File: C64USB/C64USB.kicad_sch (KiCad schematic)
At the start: 31 parts, among them J1 Keyboard, J2 USB_B_Micro, J3 AVR-ISP-6, J4 Joystick1, J5 Joystick2, J6 LED, U2 ATmega88-20A, Y1 16MHz

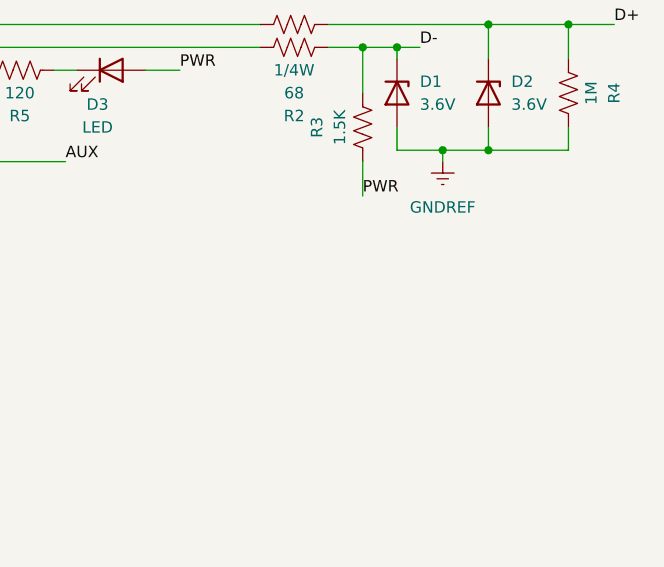
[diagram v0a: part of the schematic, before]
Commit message: Clamp D- pull up voltage
Clamps the D- pull up to ~3.3V using the simple technique of two
1N4148 diodes. Some USB host controllers are sensitive to the D- line
being pulled up to 5V (even with the 1.5K pull up resistor) and will
refuse to enumerate the device if it does so. For some reason, the TVS
diodes are not clamping the output to 3.6V.

This was particularly noticed when using the board with a Raspberry Pi
4.
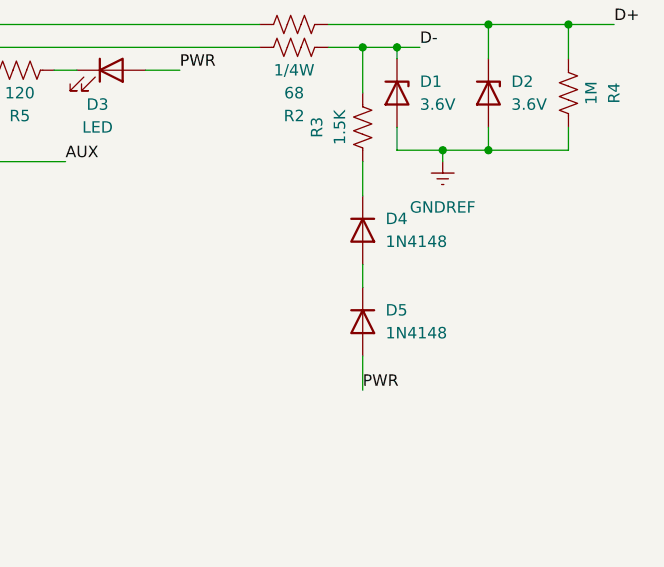
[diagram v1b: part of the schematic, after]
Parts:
- added D4, D5: 1N4148, Diode_SMD:D_SOD-123, symbol Device:D
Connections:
- net PWR: now also D5.2 (A); no longer R3.2
- new net: D4.1 (K), R3.2
- new net: D4.2 (A), D5.1 (K)
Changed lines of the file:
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@@
 	(wire
 		(pts
+			(xy 247.65 140.97) (xy 247.65 143.51)
+		)
+		(stroke
+			(width 0)
+			(type default)
+		)
+	)
+	(wire
+		(pts
 			(xy 213.36 46.99) (xy 213.36 49.53)
 		)
@@
 	(wire
 		(pts
+			(xy 247.65 151.13) (xy 247.65 154.94)
+		)
+		(stroke
+			(width 0)
+			(type default)
+		)
+	)
+	(wire
+		(pts
 			(xy 270.51 114.3) (xy 275.59 114.3)
 		)
@@
 	)
 	(label "PWR"
-		(at 247.65 133.35 0)
+		(at 247.65 154.94 0)
 		(fields_autoplaced yes)
 		(effects
@@
 		(length 2.54)
 		(shape round)
+		(at 247.65 132.08 270)
+		(fields_autoplaced yes)
+		(effects
+			(font
+				(size 1.27 1.27)
+			)
+			(justify right bottom)
+		)
+		(property "Netclass" "Power"
+			(at 250.19 131.3815 90)
+			(effects
+				(font
+					(size 1.27 1.27)
+					(italic yes)
+				)
+				(justify left)
+			)
+		)
+	)
+	(netclass_flag ""
+		(length 2.54)
+		(shape round)
+		(at 247.65 143.51 90)
+		(fields_autoplaced yes)
+		(effects
+			(font
+				(size 1.27 1.27)
+			)
+			(justify left bottom)
+		)
+		(property "Netclass" "Power"
+			(at 245.11 142.8115 90)
+			(effects
+				(font
+					(size 1.27 1.27)
+					(italic yes)
+				)
+				(justify left)
+			)
+		)
+	)
+	(netclass_flag ""
+		(length 2.54)
+		(shape round)
 		(at 220.98 31.75 0)
 		(fields_autoplaced yes)
@@
 	)
 	(symbol
+		(lib_id "Device:D")
+		(at 247.65 137.16 270)
+		(unit 1)
+		(exclude_from_sim no)
+		(in_bom yes)
+		(on_board yes)
+		(dnp no)
+		(fields_autoplaced yes)
+		(property "Reference" "D4"
+			(at 250.19 135.8899 90)
+			(effects
+				(font
+					(size 1.27 1.27)
+				)
+				(justify left)
+			)
+		)
+		(property "Value" "1N4148"
+			(at 250.19 138.4299 90)
+			(effects
+				(font
+					(size 1.27 1.27)
+				)
+				(justify left)
+			)
+		)
+		(property "Footprint" "Diode_SMD:D_SOD-123"
+			(at 247.65 137.16 0)
+			(effects
+				(font
+					(size 1.27 1.27)
+				)
+				(hide yes)
+			)
+		)
+		(property "Datasheet" "~"
+			(at 247.65 137.16 0)
+			(effects
+				(font
+					(size 1.27 1.27)
+				)
+				(hide yes)
+			)
+		)
+		(property "Description" "Diode"
+			(at 247.65 137.16 0)
+			(effects
+				(font
+					(size 1.27 1.27)
+				)
+				(hide yes)
+			)
+		)
+		(property "Sim.Device" "D"
+			(at 247.65 137.16 0)
+			(effects
+				(font
+					(size 1.27 1.27)
+				)
+				(hide yes)
+			)
+		)
+		(property "Sim.Pins" "1=K 2=A"
+			(at 247.65 137.16 0)
+			(effects
+				(font
+					(size 1.27 1.27)
+				)
+				(hide yes)
+			)
+		)
+		(pin "2"
+		)
+		(pin "1"
+		)
+		(instances
+			(project ""
+				(path "/683b04d7-2177-49fe-8cac-bb0e8fe56ae0"
+					(reference "D4")
+					(unit 1)
+				)
+			)
+		)
+	)
+	(symbol
 		(lib_id "Mechanical:MountingHole")
 		(at 16.51 165.1 0)
@@
 					(unit 1)
 				)
+			)
+		)
+	)
+	(symbol
+		(lib_id "Device:D")
+		(at 247.65 147.32 270)
+		(unit 1)
+		(exclude_from_sim no)
+		(in_bom yes)
+		(on_board yes)
+		(dnp no)
+		(fields_autoplaced yes)
+		(property "Reference" "D5"
+			(at 250.19 146.0499 90)
+			(effects
+				(font
+					(size 1.27 1.27)
+				)
+				(justify left)
+			)
+		)
+		(property "Value" "1N4148"
+			(at 250.19 148.5899 90)
+			(effects
+				(font
+					(size 1.27 1.27)
+				)
+				(justify left)
+			)
+		)
+		(property "Footprint" "Diode_SMD:D_SOD-123"
+			(at 247.65 147.32 0)
+			(effects
+				(font
+					(size 1.27 1.27)
+				)
+				(hide yes)
+			)
+		)
+		(property "Datasheet" "~"
+			(at 247.65 147.32 0)
+			(effects
+				(font
+					(size 1.27 1.27)
+				)
+				(hide yes)
+			)
+		)
+		(property "Description" "Diode"
+			(at 247.65 147.32 0)
+			(effects
+				(font
+					(size 1.27 1.27)
+				)
+				(hide yes)
+			)
+		)
+		(property "Sim.Device" "D"
+			(at 247.65 147.32 0)
+			(effects
+				(font
+					(size 1.27 1.27)
+				)
+				(hide yes)
+			)
+		)
+		(property "Sim.Pins" "1=K 2=A"
+			(at 247.65 147.32 0)
+			(effects
+				(font
+					(size 1.27 1.27)
+				)
+				(hide yes)
+			)
+		)
+		(pin "2"
+		)
+		(pin "1"
+		)
+		(instances
+			(project "C64USB"
+				(path "/683b04d7-2177-49fe-8cac-bb0e8fe56ae0"
+					(reference "D5")
+					(unit 1)
+				)

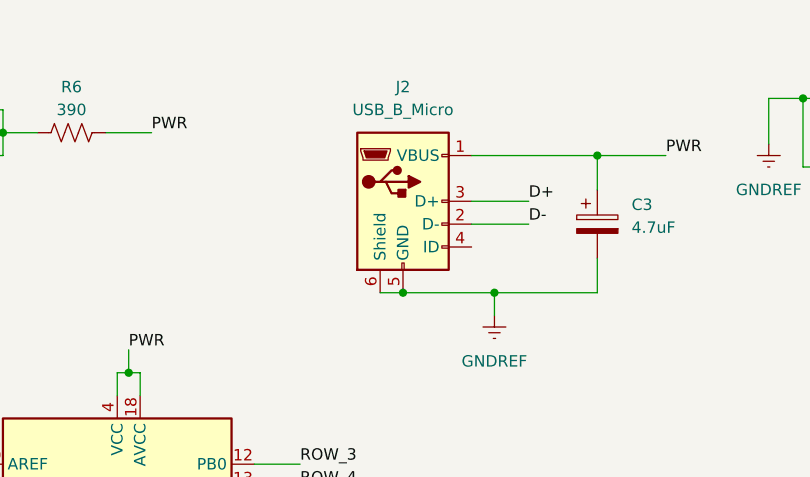
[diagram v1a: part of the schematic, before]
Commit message: Replace micro-USB connector with USB-B
The micro USB connector is very difficult to solder correctly, so
replace it with a USB-B connector which should be much easier
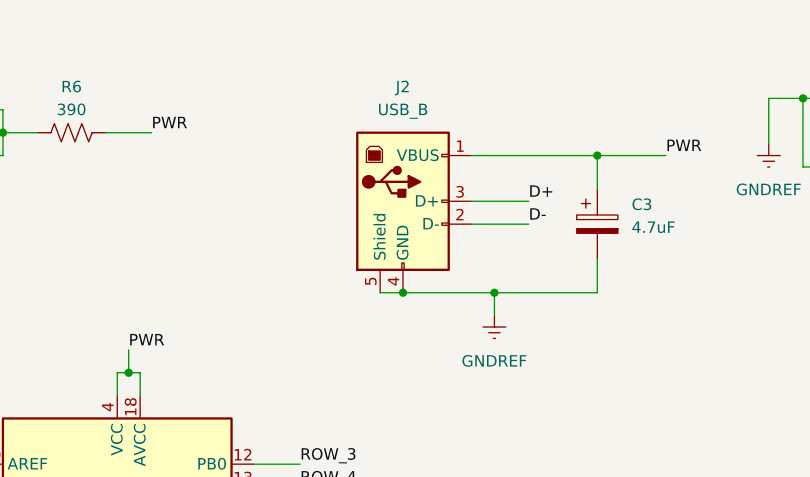
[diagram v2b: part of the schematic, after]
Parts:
- removed J2: USB_B_Micro, Connector_USB:USB_Micro-B_Wuerth_629105150521, symbol Connector:USB_B_Micro
- added J2: USB_B, Connector_USB:USB_B_Lumberg_2411_02_Horizontal, symbol Connector:USB_B
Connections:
- net D+: now also J2.3 (D+)
- net D-: now also J2.2 (D-)
- net GNDREF: now also J2.4 (GND), J2.5 (Shield)
- net PWR: now also J2.1 (VBUS)
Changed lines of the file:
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@@
 	)
 	(junction
-		(at 247.65 25.4)
+		(at 203.2 46.99)
 		(diameter 0)
 		(color 0 0 0 0)
 	)
 	(junction
-		(at 261.62 114.3)
+		(at 247.65 25.4)
 		(diameter 0)
 		(color 0 0 0 0)
 	)
 	(junction
-		(at 224.79 31.75)
+		(at 261.62 114.3)
 		(diameter 0)
 		(color 0 0 0 0)
 	)
 	(junction
-		(at 203.2 46.99)
+		(at 224.79 31.75)
 		(diameter 0)
 		(color 0 0 0 0)
@@
 	(wire
 		(pts
-			(xy 186.69 104.14) (xy 191.77 104.14)
+			(xy 200.66 46.99) (xy 203.2 46.99)
 		)
 		(stroke
@@
 	(wire
 		(pts
-			(xy 203.2 129.54) (xy 203.2 119.38)
+			(xy 186.69 104.14) (xy 191.77 104.14)
 		)
 		(stroke
@@
 	(wire
 		(pts
-			(xy 247.65 25.4) (xy 243.84 25.4)
+			(xy 203.2 129.54) (xy 203.2 119.38)
 		)
 		(stroke
@@
 	(wire
 		(pts
-			(xy 203.2 46.99) (xy 213.36 46.99)
+			(xy 247.65 25.4) (xy 243.84 25.4)
 		)
 		(stroke
@@
 	(wire
 		(pts
-			(xy 200.66 46.99) (xy 203.2 46.99)
-		)
-		(stroke
-			(width 0)
-			(type default)
-		)
-	)
-	(wire
-		(pts
 			(xy 50.8 144.78) (xy 73.66 144.78)
 		)
@@
 	(wire
 		(pts
+			(xy 203.2 46.99) (xy 213.36 46.99)
+		)
+		(stroke
+			(width 0)
+			(type default)
+		)
+	)
+	(wire
+		(pts
 			(xy 224.79 31.75) (xy 224.79 35.56)
 		)
@@
 	)
 	(symbol
+		(lib_id "Connector:USB_B")
+		(at 203.2 36.83 0)
+		(unit 1)
+		(exclude_from_sim no)
+		(in_bom yes)
+		(on_board yes)
+		(dnp no)
+		(fields_autoplaced yes)
+		(property "Reference" "J2"
+			(at 203.2 24.13 0)
+			(effects
+				(font
+					(size 1.27 1.27)
+				)
+			)
+		)
+		(property "Value" "USB_B"
+			(at 203.2 26.67 0)
+			(effects
+				(font
+					(size 1.27 1.27)
+				)
+			)
+		)
+		(property "Footprint" "Connector_USB:USB_B_Lumberg_2411_02_Horizontal"
+			(at 207.01 38.1 0)
+			(effects
+				(font
+					(size 1.27 1.27)
+				)
+				(hide yes)
+			)
+		)
+		(property "Datasheet" "~"
+			(at 207.01 38.1 0)
+			(effects
+				(font
+					(size 1.27 1.27)
+				)
+				(hide yes)
+			)
+		)
+		(property "Description" "USB Type B connector"
+			(at 203.2 36.83 0)
+			(effects
+				(font
+					(size 1.27 1.27)
+				)
+				(hide yes)
+			)
+		)
+		(pin "2"
+		)
+		(pin "4"
+		)
+		(pin "3"
+		)
+		(pin "1"
+		)
+		(pin "5"
+		)
+		(instances
+			(project ""
+				(path "/683b04d7-2177-49fe-8cac-bb0e8fe56ae0"
+					(reference "J2")
+					(unit 1)
+				)
+			)
+		)
+	)
+	(symbol
 		(lib_id "Connector:Conn_01x03_Pin")
 		(at 143.51 29.21 0)
@@
 					(unit 1)
 				)
-			)
-		)
-	)
-	(symbol
-		(lib_id "Connector:USB_B_Micro")
-		(at 203.2 36.83 0)
-		(unit 1)
-		(exclude_from_sim no)
-		(in_bom yes)
-		(on_board yes)
-		(dnp no)
-		(fields_autoplaced yes)
-		(property "Reference" "J2"
-			(at 203.2 24.13 0)
-			(effects
-				(font
-					(size 1.27 1.27)
-				)
-			)
-		)
-		(property "Value" "USB_B_Micro"
-			(at 203.2 26.67 0)
-			(effects
-				(font
-					(size 1.27 1.27)
-				)
-			)
-		)
-		(property "Footprint" "Connector_USB:USB_Micro-B_Wuerth_629105150521"
-			(at 207.01 38.1 0)
-			(effects
-				(font
-					(size 1.27 1.27)
-				)
-				(hide yes)
-			)
-		)
-		(property "Datasheet" "~"
-			(at 207.01 38.1 0)
-			(effects
-				(font
-					(size 1.27 1.27)
-				)
-				(hide yes)
-			)
-		)
-		(property "Description" "USB Micro Type B connector"
-			(at 203.2 36.83 0)
-			(effects
-				(font
-					(size 1.27 1.27)
-				)
-				(hide yes)
-			)
-		)
-		(pin "6"
-		)
-		(pin "2"
-		)
-		(pin "5"
-		)
-		(pin "3"
-		)
-		(pin "1"
-		)
-		(pin "4"
-		)
-		(instances
-			(project ""
-				(path "/683b04d7-2177-49fe-8cac-bb0e8fe56ae0"
-					(reference "J2")
-					(unit 1)
-				)

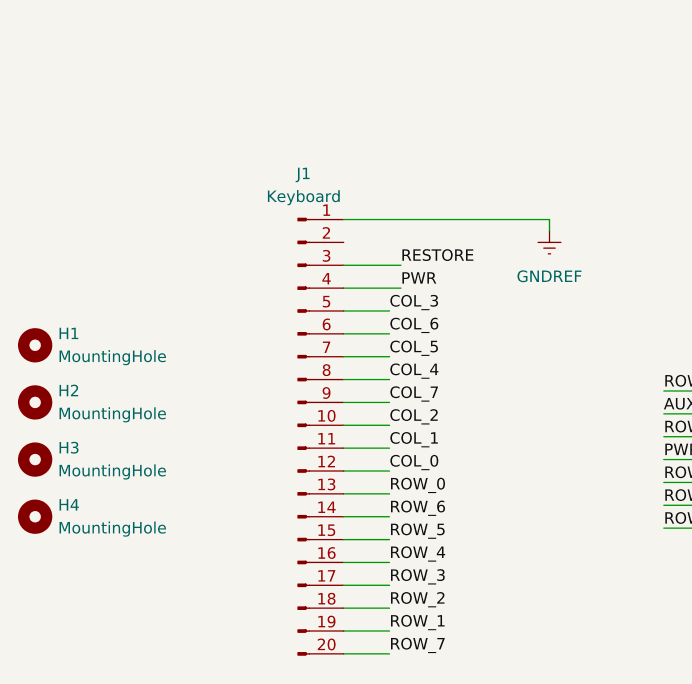
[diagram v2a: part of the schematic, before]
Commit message: Use custom symbol and footprint for keyboard header
This one correctly omits the key pin
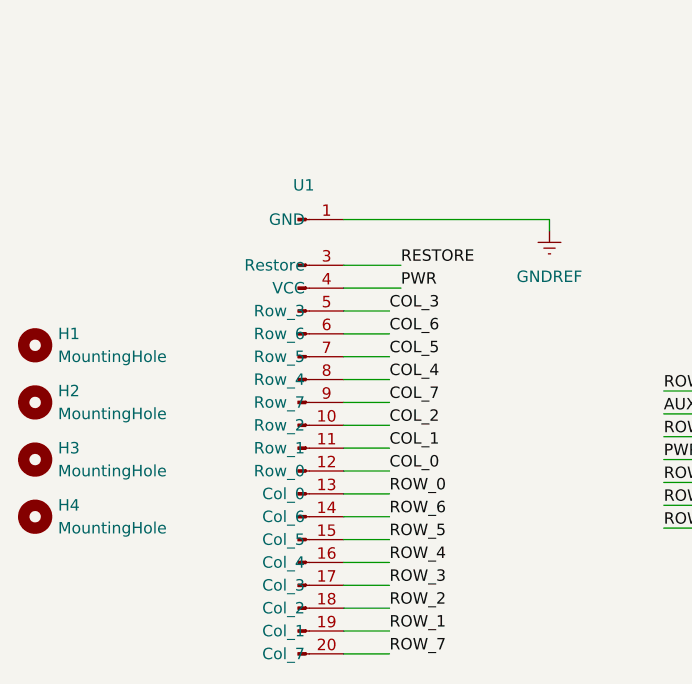
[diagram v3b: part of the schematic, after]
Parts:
- removed J1: Keyboard, Connector_PinHeader_2.54mm:PinHeader_1x20_P2.54mm_Vertical, symbol Connector:Conn_01x20_Pin
- added U1: ~, C64:C64_Keyboard_Header, symbol C64:C64_Keyboard
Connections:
- net COL_0: now also U1.12 (Row_0)
- net COL_1: now also U1.11 (Row_1)
- net COL_2: now also U1.10 (Row_2)
- net COL_3: now also U1.5 (Row_3)
- net COL_4: now also U1.8 (Row_4)
- net COL_5: now also U1.7 (Row_5)
- net COL_6: now also U1.6 (Row_6)
- net COL_7: now also U1.9 (Row_7)
- net GNDREF: now also U1.1 (GND)
- net PWR: now also U1.4 (VCC)
- net RESTORE: now also U1.3 (Restore)
- net ROW_0: now also U1.13 (Col_0)
- net ROW_1: now also U1.19 (Col_1)
- net ROW_2: now also U1.18 (Col_2)
- net ROW_3: now also U1.17 (Col_3)
- net ROW_4: now also U1.16 (Col_4)
- net ROW_5: now also U1.15 (Col_5)
- net ROW_6: now also U1.14 (Col_6)
- net ROW_7: now also U1.20 (Col_7)
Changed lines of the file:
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@@
-	)
-	(symbol
-		(lib_id "Connector:Conn_01x20_Pin")
-		(at 45.72 167.64 0)
-		(unit 1)
-		(exclude_from_sim no)
-		(in_bom yes)
-		(on_board yes)
-		(dnp no)
-		(fields_autoplaced yes)
-		(property "Reference" "J1"
-			(at 46.355 139.7 0)
-			(effects
-				(font
-					(size 1.27 1.27)
-				)
-			)
-		)
-		(property "Value" "Keyboard"
-			(at 46.355 142.24 0)
-			(effects
-				(font
-					(size 1.27 1.27)
-				)
-			)
-		)
-		(property "Footprint" "Connector_PinHeader_2.54mm:PinHeader_1x20_P2.54mm_Vertical"
-			(at 45.72 167.64 0)
-			(effects
-				(font
-					(size 1.27 1.27)
-				)
-				(hide yes)
-			)
-		)
-		(property "Datasheet" "~"
-			(at 45.72 167.64 0)
-			(effects
-				(font
-					(size 1.27 1.27)
-				)
-				(hide yes)
-			)
-		)
-		(property "Description" "Generic connector, single row, 01x20, script generated"
-			(at 45.72 167.64 0)
-			(effects
-				(font
-					(size 1.27 1.27)
-				)
-				(hide yes)
-			)
-		)
-		(pin "7"
-		)
-		(pin "6"
-		)
-		(pin "13"
-		)
-		(pin "11"
-		)
-		(pin "12"
-		)
-		(pin "18"
-		)
-		(pin "2"
-		)
-		(pin "17"
-		)
-		(pin "5"
-		)
-		(pin "4"
-		)
-		(pin "20"
-		)
-		(pin "16"
-		)
-		(pin "19"
-		)
-		(pin "10"
-		)
-		(pin "14"
-		)
-		(pin "1"
-		)
-		(pin "9"
-		)
-		(pin "3"
-		)
-		(pin "8"
-		)
-		(pin "15"
-		)
-		(instances
-			(project ""
-				(path "/683b04d7-2177-49fe-8cac-bb0e8fe56ae0"
-					(reference "J1")
-					(unit 1)
-				)
-			)
-		)
 	)
 	(symbol
@@
 					(unit 1)
 				)
+			)
+		)
+	)
+	(symbol
+		(lib_id "C64:C64_Keyboard")
+		(at 50.8 142.24 0)
+		(unit 1)
+		(exclude_from_sim no)
+		(in_bom yes)
+		(on_board yes)
+		(dnp no)
+		(fields_autoplaced yes)
+		(property "Reference" "U1"
+			(at 46.355 140.97 0)
+			(effects
+				(font
+					(size 1.27 1.27)
+				)
+			)
+		)
+		(property "Value" "~"
+			(at 46.355 143.51 0)
+			(effects
+				(font
+					(size 1.27 1.27)
+				)
+			)
+		)
+		(property "Footprint" "C64:C64_Keyboard_Header"
+			(at 50.8 195.834 0)
+			(effects
+				(font
+					(size 1.27 1.27)
+				)
+				(hide yes)
+			)
+		)
+		(property "Datasheet" ""
+			(at 50.8 142.24 0)
+			(effects
+				(font
+					(size 1.27 1.27)
+				)
+				(hide yes)
+			)
+		)
+		(property "Description" ""
+			(at 50.8 142.24 0)
+			(effects
+				(font
+					(size 1.27 1.27)
+				)
+				(hide yes)
+			)
+		)
+		(pin "20"
+		)
+		(pin "19"
+		)
+		(pin "9"
+		)
+		(pin "4"
+		)
+		(pin "8"
+		)
+		(pin "18"
+		)
+		(pin "12"
+		)
+		(pin "1"
+		)
+		(pin "10"
+		)
+		(pin "16"
+		)
+		(pin "14"
+		)
+		(pin "15"
+		)
+		(pin "13"
+		)
+		(pin "11"
+		)
+		(pin "3"
+		)
+		(pin "6"
+		)
+		(pin "7"
+		)
+		(pin "5"
+		)
+		(pin "17"
+		)
+		(instances
+			(project ""
+				(path "/683b04d7-2177-49fe-8cac-bb0e8fe56ae0"
+					(reference "U1")
+					(unit 1)
+				)

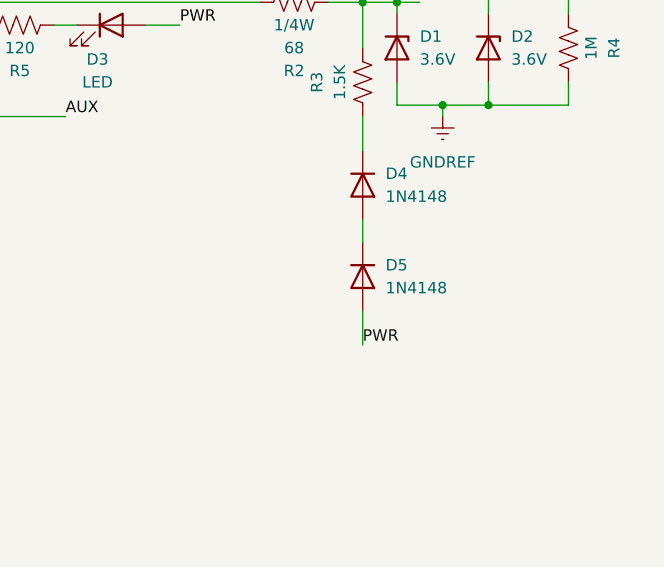
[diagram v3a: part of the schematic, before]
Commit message: Remove one diode from D-
After further testing, a single diode is sufficient to allow the device
to enumerate on the problematic USB controllers. This leads me to
believe that this means the controller is actually detecting the device
being back-powered through D-, which makes a lot more sense, and the
Zener diode is sufficiently clamping the voltage
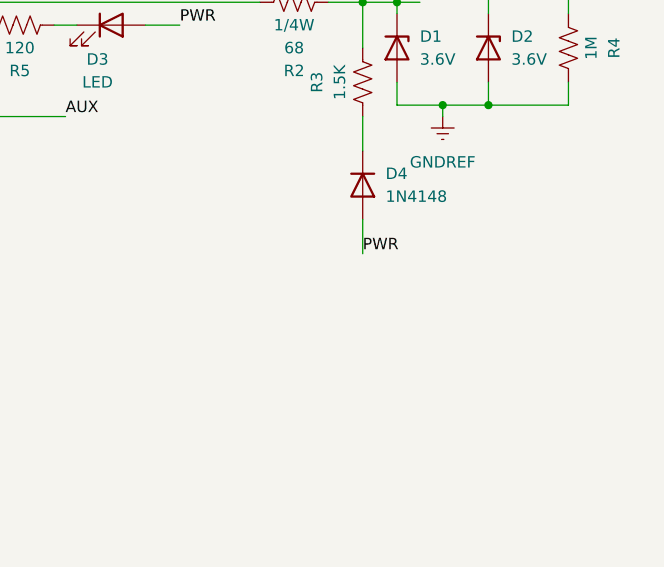
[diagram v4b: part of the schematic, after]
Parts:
- removed D5: 1N4148, Diode_SMD:D_SOD-123, symbol Device:D
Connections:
- net PWR: now also D4.2 (A)
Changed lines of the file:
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@@
 	(wire
 		(pts
-			(xy 247.65 140.97) (xy 247.65 143.51)
-		)
-		(stroke
-			(width 0)
-			(type default)
-		)
-	)
-	(wire
-		(pts
 			(xy 213.36 46.99) (xy 213.36 49.53)
 		)
@@
 	(wire
 		(pts
-			(xy 247.65 151.13) (xy 247.65 154.94)
+			(xy 247.65 140.97) (xy 247.65 144.78)
 		)
 		(stroke
@@
 	)
 	(label "PWR"
-		(at 247.65 154.94 0)
+		(at 247.65 144.78 0)
 		(fields_autoplaced yes)
 		(effects
@@
 		(length 2.54)
 		(shape round)
-		(at 247.65 132.08 270)
-		(fields_autoplaced yes)
-		(effects
-			(font
-				(size 1.27 1.27)
-			)
-			(justify right bottom)
-		)
-		(property "Netclass" "Power"
-			(at 250.19 131.3815 90)
-			(effects
-				(font
-					(size 1.27 1.27)
-					(italic yes)
-				)
-				(justify left)
-			)
-		)
-	)
-	(netclass_flag ""
-		(length 2.54)
-		(shape round)
-		(at 247.65 143.51 90)
-		(fields_autoplaced yes)
-		(effects
-			(font
-				(size 1.27 1.27)
-			)
-			(justify left bottom)
-		)
-		(property "Netclass" "Power"
-			(at 245.11 142.8115 90)
-			(effects
-				(font
-					(size 1.27 1.27)
-					(italic yes)
-				)
-				(justify left)
-			)
-		)
-	)
-	(netclass_flag ""
-		(length 2.54)
-		(shape round)
 		(at 220.98 31.75 0)
 		(fields_autoplaced yes)
@@
 					(unit 1)
 				)
-			)
-		)
-	)
-	(symbol
-		(lib_id "Device:D")
-		(at 247.65 147.32 270)
-		(unit 1)
-		(exclude_from_sim no)
-		(in_bom yes)
-		(on_board yes)
-		(dnp no)
-		(fields_autoplaced yes)
-		(property "Reference" "D5"
-			(at 250.19 146.0499 90)
-			(effects
-				(font
-					(size 1.27 1.27)
-				)
-				(justify left)
-			)
-		)
-		(property "Value" "1N4148"
-			(at 250.19 148.5899 90)
-			(effects
-				(font
-					(size 1.27 1.27)
-				)
-				(justify left)
-			)
-		)
-		(property "Footprint" "Diode_SMD:D_SOD-123"
-			(at 247.65 147.32 0)
-			(effects
-				(font
-					(size 1.27 1.27)
-				)
-				(hide yes)
-			)
-		)
-		(property "Datasheet" "~"
-			(at 247.65 147.32 0)
-			(effects
-				(font
-					(size 1.27 1.27)
-				)
-				(hide yes)
-			)
-		)
-		(property "Description" "Diode"
-			(at 247.65 147.32 0)
-			(effects
-				(font
-					(size 1.27 1.27)
-				)
-				(hide yes)
-			)
-		)
-		(property "Sim.Device" "D"
-			(at 247.65 147.32 0)
-			(effects
-				(font
-					(size 1.27 1.27)
-				)
-				(hide yes)
-			)
-		)
-		(property "Sim.Pins" "1=K 2=A"
-			(at 247.65 147.32 0)
-			(effects
-				(font
-					(size 1.27 1.27)
-				)
-				(hide yes)
-			)
-		)
-		(pin "2"
-		)
-		(pin "1"
-		)
-		(instances
-			(project "C64USB"
-				(path "/683b04d7-2177-49fe-8cac-bb0e8fe56ae0"
-					(reference "D5")
-					(unit 1)
-				)
